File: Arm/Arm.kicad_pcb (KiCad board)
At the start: 2 copper layers, 91.1 x 109 mm, 88 parts, among them J10 SparkMAX XT60 F, J11 CAN OUT, J12 SparkMAX XT60 F, J13 SparkMAX XT60 F, J14 Encoder 0, J2 Encoder Bundle, J3 CAN IN, J4 5V Swtich Power, J5 Power IN XT60 M, J6 SparkMAX XT60 F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

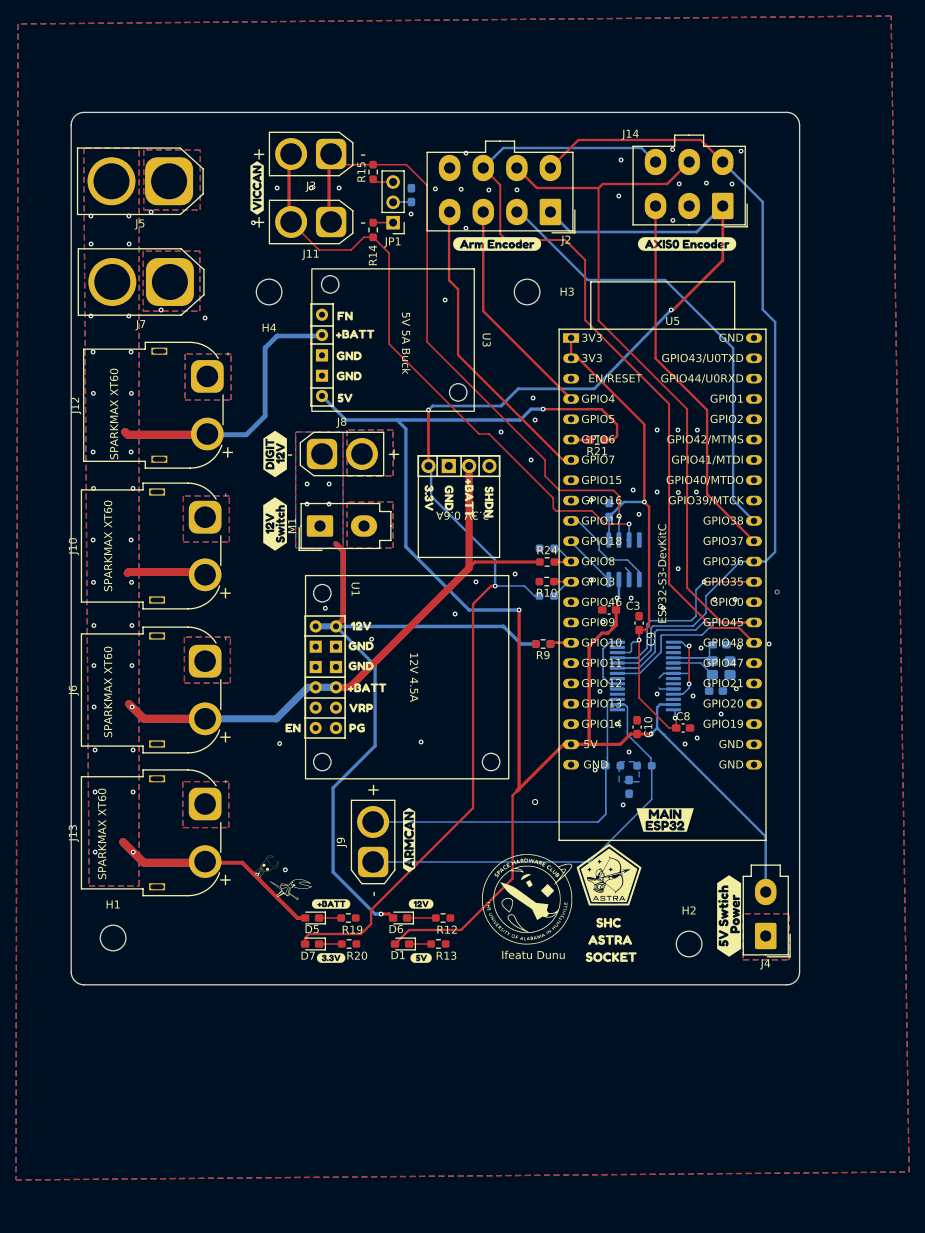
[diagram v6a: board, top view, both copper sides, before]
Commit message: Moving Connectors and small layout changes
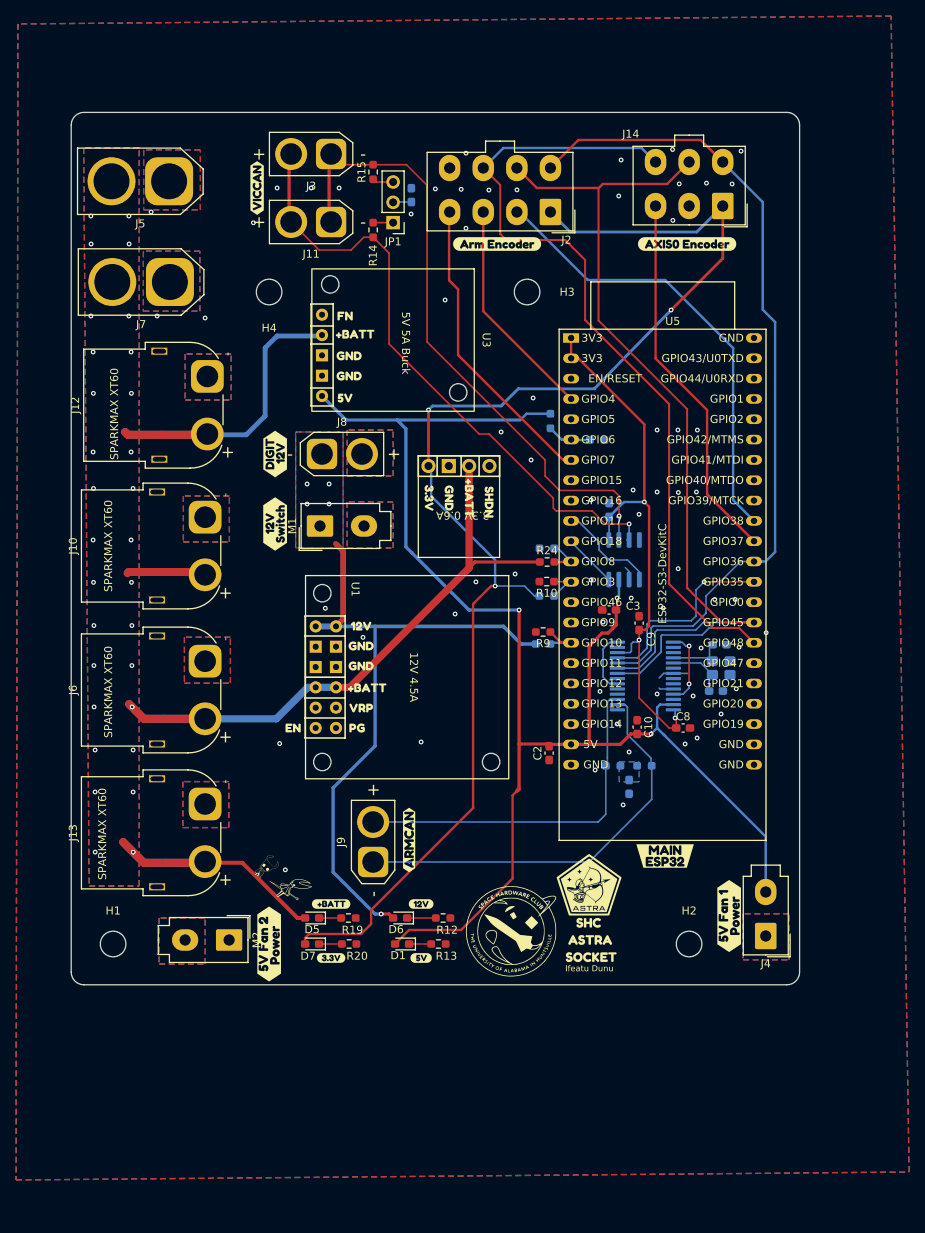
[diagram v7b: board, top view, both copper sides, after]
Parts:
- removed kibuzzard-69826405: G***, kibuzzard-69826405
- added C2: C_Small, Capacitor_SMD:C_0603_1608Metric_Pad1.08x0.95mm_HandSolder, F.Cu at (105.5, 131.6)
- added M2: Fan, Connector_Molex:Molex_Mini-Fit_Jr_5566-02A_2x01_P4.20mm_Vertical, F.Cu at (65.5, 155.0)
- added kibuzzard-698ABA0B: G***, kibuzzard-698ABA0B, F.Cu at (128.0, 152.0)
- added kibuzzard-69920ED8: G***, kibuzzard-69920ED8, F.Cu at (70.5, 155.5)
- R21: moved to B.Cu
- moved R21 6.30 mm to (105.7, 90.1), turned to -90 degrees
- moved kibuzzard-69783B26 4.50 mm to (120.0, 144.5)
- moved G*** 4.47 mm to (101.0, 154.0)
- moved G*** 2.80 mm to (110.5, 148.0)
- moved kibuzzard-69701E52 2.50 mm to (110.8, 155.0)
- moved R9 1.50 mm to (104.8, 116.5)
- moved H1 0.75 mm to (51.0, 155.5)
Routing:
- net +5V: track 202.1 -> 187.4 mm, vias 4 -> 3
- net +12V: track 95.3 -> 93.3 mm
- net /5V_ADC: track 4.72 -> 5.60 mm
- net GND: vias 67 -> 64

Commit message: 1/3 Final Changes
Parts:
- removed kibuzzard-69920ED8: G***, kibuzzard-69920ED8
- added kibuzzard-699F8EAF: G***, kibuzzard-699F8EAF, F.Cu at (70.5, 155.5)
- moved R12 18.5 mm to (74.5, 157.1), turned to 90 degrees
- moved kibuzzard-6970222E 16.5 mm to (75.7, 159.6)
- moved D6 11.2 mm to (76.7, 157.1), turned to 90 degrees
- moved R13 10.3 mm to (81.5, 157.2), turned to 90 degrees
- moved D7 8.51 mm to (83.7, 152.3), turned to 90 degrees
- moved kibuzzard-696EF04A 7.50 mm to (82.4, 159.6)
- moved R19 5.97 mm to (74.4, 152.2), turned to 90 degrees
- moved kibuzzard-69702208 5.07 mm to (82.6, 154.7)
- moved kibuzzard-696EF05A 4.90 mm to (75.6, 154.6)
- moved J9 4.13 mm to (87.6, 145.0)
- moved kibuzzard-6970240E 4.13 mm to (92.1, 142.2)
- moved D1 3.79 mm to (83.7, 157.1), turned to 90 degrees
- moved R20 3.41 mm to (81.5, 152.2), turned to 90 degrees
- moved D5 0.91 mm to (76.8, 152.2), turned to 90 degrees
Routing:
- net +12V: track 93.3 -> 112.5 mm
- net +3.3V: track 167.4 -> 157.9 mm
- net /MISO_ESP0: track 109.6 -> 114.7 mm
- net /CLK_ESP0: track 124.3 -> 129.3 mm
- net /MOSI_ESP0: track 103.9 -> 106.9 mm
- net +5V: track 187.4 -> 190.3 mm
- net /CS_Motor_CAN: track 24.7 -> 27.2 mm
- net /CS_Encoder_1: track 56.8 -> 59.3 mm
- net /CS_Encoder_0: track 47.0 -> 49.5 mm
- net +BATT: track 186.8 -> 188.2 mm
- net Net-(D6-K): track 3.59 -> 2.31 mm
- net Net-(D7-K): track 2.84 -> 2.25 mm
- net Net-(D1-K): track 2.75 -> 2.25 mm
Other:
- board size 91.1 x 109 mm -> 92.4 x 109 mm
